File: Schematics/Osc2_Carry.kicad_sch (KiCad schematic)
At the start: 55 parts, among them J40 Conn_01x04, J41 Conn_01x02, J42 Conn_01x02, J43 Screw_Terminal_01x03, J44 Screw_Terminal_01x03, J45 Conn_01x04, U21 MCP4728, U22 MCP4728, U23 TL072, U24 LM358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

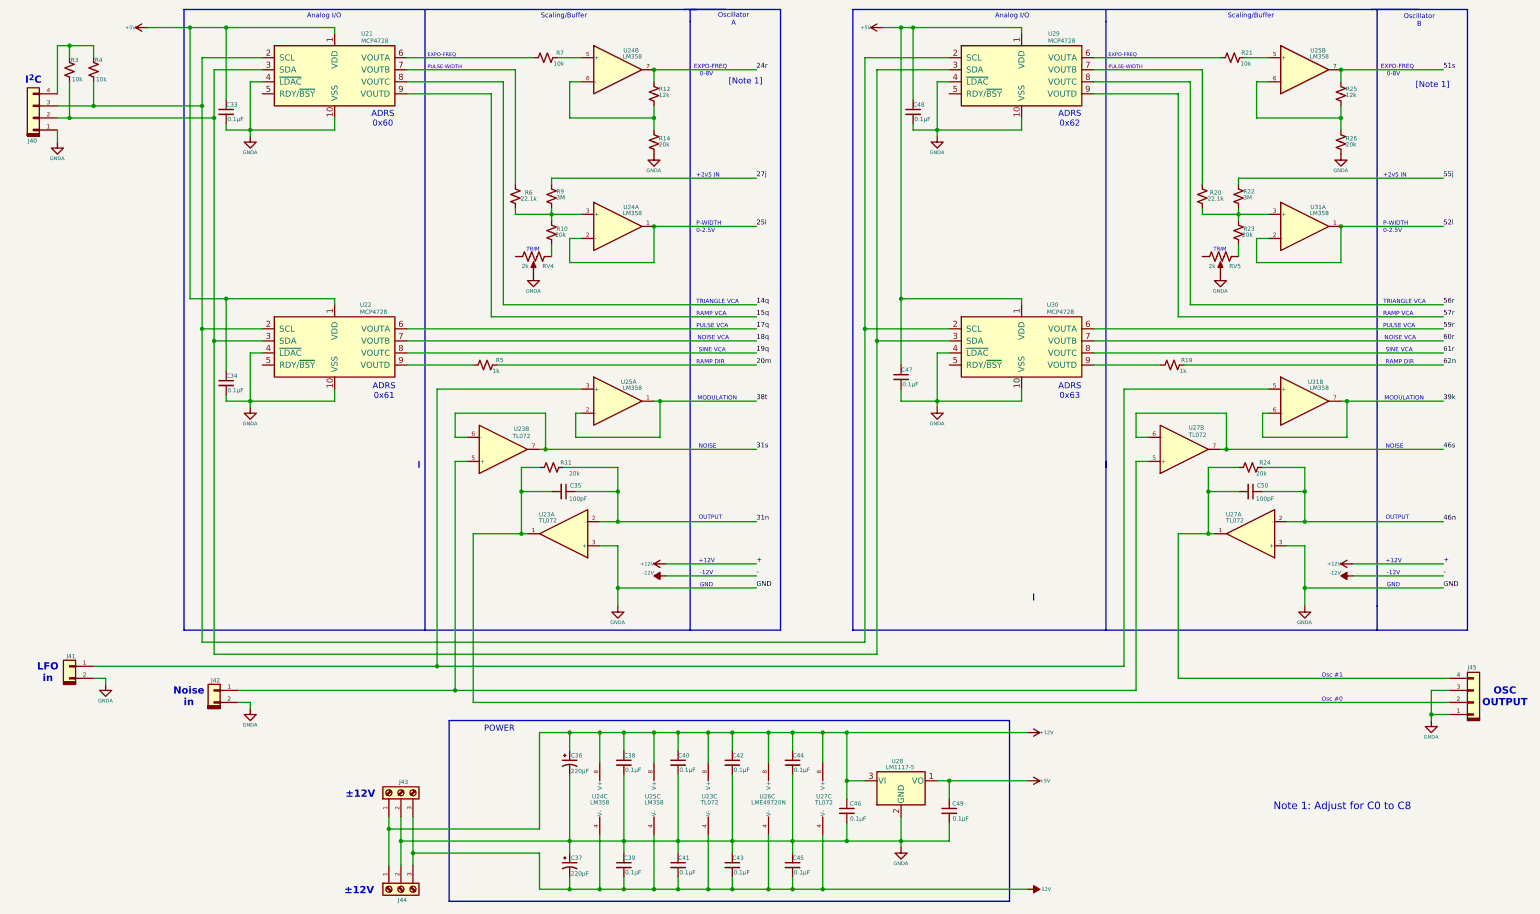
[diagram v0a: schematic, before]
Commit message: Updated schematics and added low pass filter and new filter mux.
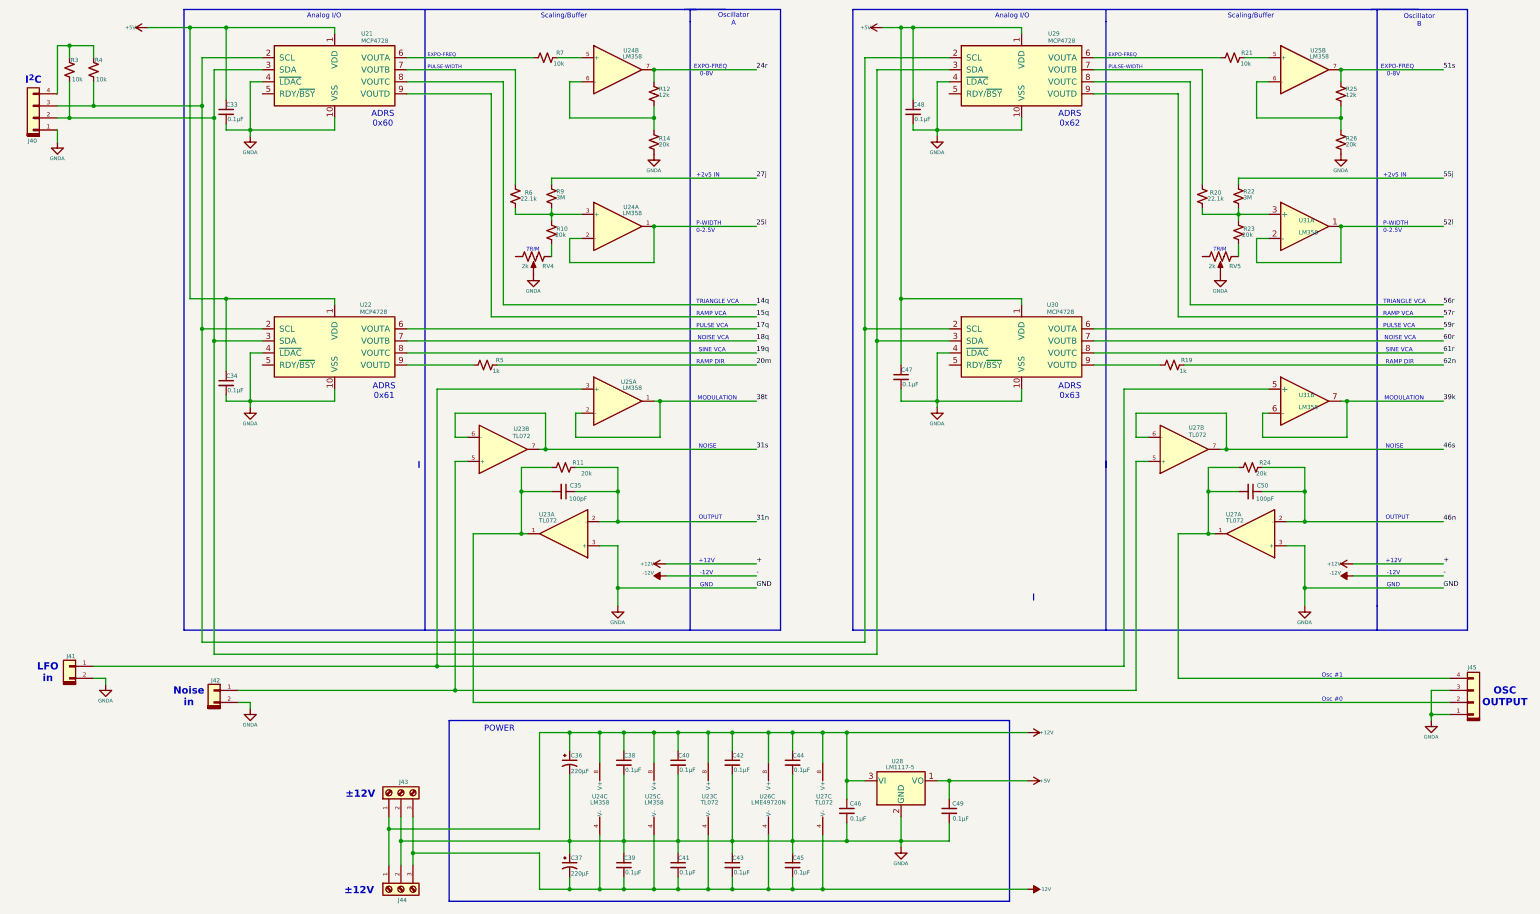
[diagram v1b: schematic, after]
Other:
- note removed: "Note 1: Adjust for C0 to C8"
- note removed: "[Note 1]"
- moved on the sheet: R11
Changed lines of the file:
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@@
 		)
 	)
-	(text "Note 1: Adjust for C0 to C8"
-		(exclude_from_sim no)
-		(at 279.146 181.102 0)
-		(effects
-			(font
-				(size 1.5748 1.5748)
-			)
-			(justify left top)
-		)
-	)
 	(text "_{TRIM}"
 		(exclude_from_sim no)
@@
 		)
 	)
-	(text "[Note 1]"
-		(exclude_from_sim no)
-		(at 312.674 29.972 0)
-		(effects
-			(font
-				(size 1.27 1.27)
-			)
-		)
-	)
 	(text "Osc #1"
 		(exclude_from_sim no)
@@
 		)
 	)
-	(text "[Note 1]"
-		(exclude_from_sim no)
-		(at 167.894 29.21 0)
-		(effects
-			(font
-				(size 1.27 1.27)
-			)
-		)
-	)
 	(text "+12V"
 		(exclude_from_sim no)
@@
 	(wire
 		(pts
-			(xy 124.46 110.49) (xy 120.65 110.49)
+			(xy 127 110.49) (xy 120.65 110.49)
 		)
 		(stroke
@@
 	(wire
 		(pts
-			(xy 129.54 110.49) (xy 140.97 110.49)
+			(xy 132.08 110.49) (xy 140.97 110.49)
 		)
 		(stroke
@@
 		(fields_autoplaced yes)
 		(property "Reference" "U31"
-			(at 288.036 92.456 0)
+			(at 284.48 95.25 0)
 			(effects
 				(font
 					(size 0.889 0.889)
 				)
+				(justify left)
 			)
 		)
 		(property "Value" "LM358"
-			(at 288.798 93.726 0)
+			(at 284.48 97.79 0)
 			(effects
 				(font
 					(size 0.889 0.889)
 				)
+				(justify left)
 			)
 		)
@@
 	)
 	(symbol
-		(lib_name "LM358_3")
+		(lib_name "LM358_6")
 		(lib_id "Amplifier_Operational:LM358")
 		(at 285.75 59.69 0)
@@
 		(dnp no)
 		(property "Reference" "U31"
-			(at 288.544 55.626 0)
+			(at 284.48 58.42 0)
 			(effects
 				(font
 					(size 0.889 0.889)
 				)
+				(justify left)
 			)
 		)
 		(property "Value" "LM358"
-			(at 288.798 56.896 0)
+			(at 284.48 60.96 0)
 			(effects
 				(font
 					(size 0.889 0.889)
 				)
+				(justify left)
 			)
 		)
@@
 	(symbol
 		(lib_id "Device:R_Small_US")
-		(at 127 110.49 90)
+		(at 129.54 110.49 90)
 		(unit 1)
 		(exclude_from_sim no)
@@
 		(dnp no)
 		(property "Reference" "R11"
-			(at 130.048 109.474 90)
+			(at 132.588 109.474 90)
 			(effects
 				(font
@@
 		)
 		(property "Value" "20k"
-			(at 131.826 111.76 90)
+			(at 134.366 111.76 90)
 			(effects
 				(font
@@
 		)
 		(property "Footprint" ""
-			(at 127 110.49 0)
+			(at 129.54 110.49 0)
 			(effects
 				(font
@@
 		)
 		(property "Datasheet" "~"
-			(at 127 110.49 0)
+			(at 129.54 110.49 0)
 			(effects
 				(font
@@
 		)
 		(property "Description" ""
-			(at 127 110.49 0)
+			(at 129.54 110.49 0)
 			(effects
 				(font
